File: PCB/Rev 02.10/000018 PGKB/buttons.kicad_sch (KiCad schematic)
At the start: 50 parts, among them U1 SN74HCS365PWR, U2 SN74HCS365PWR

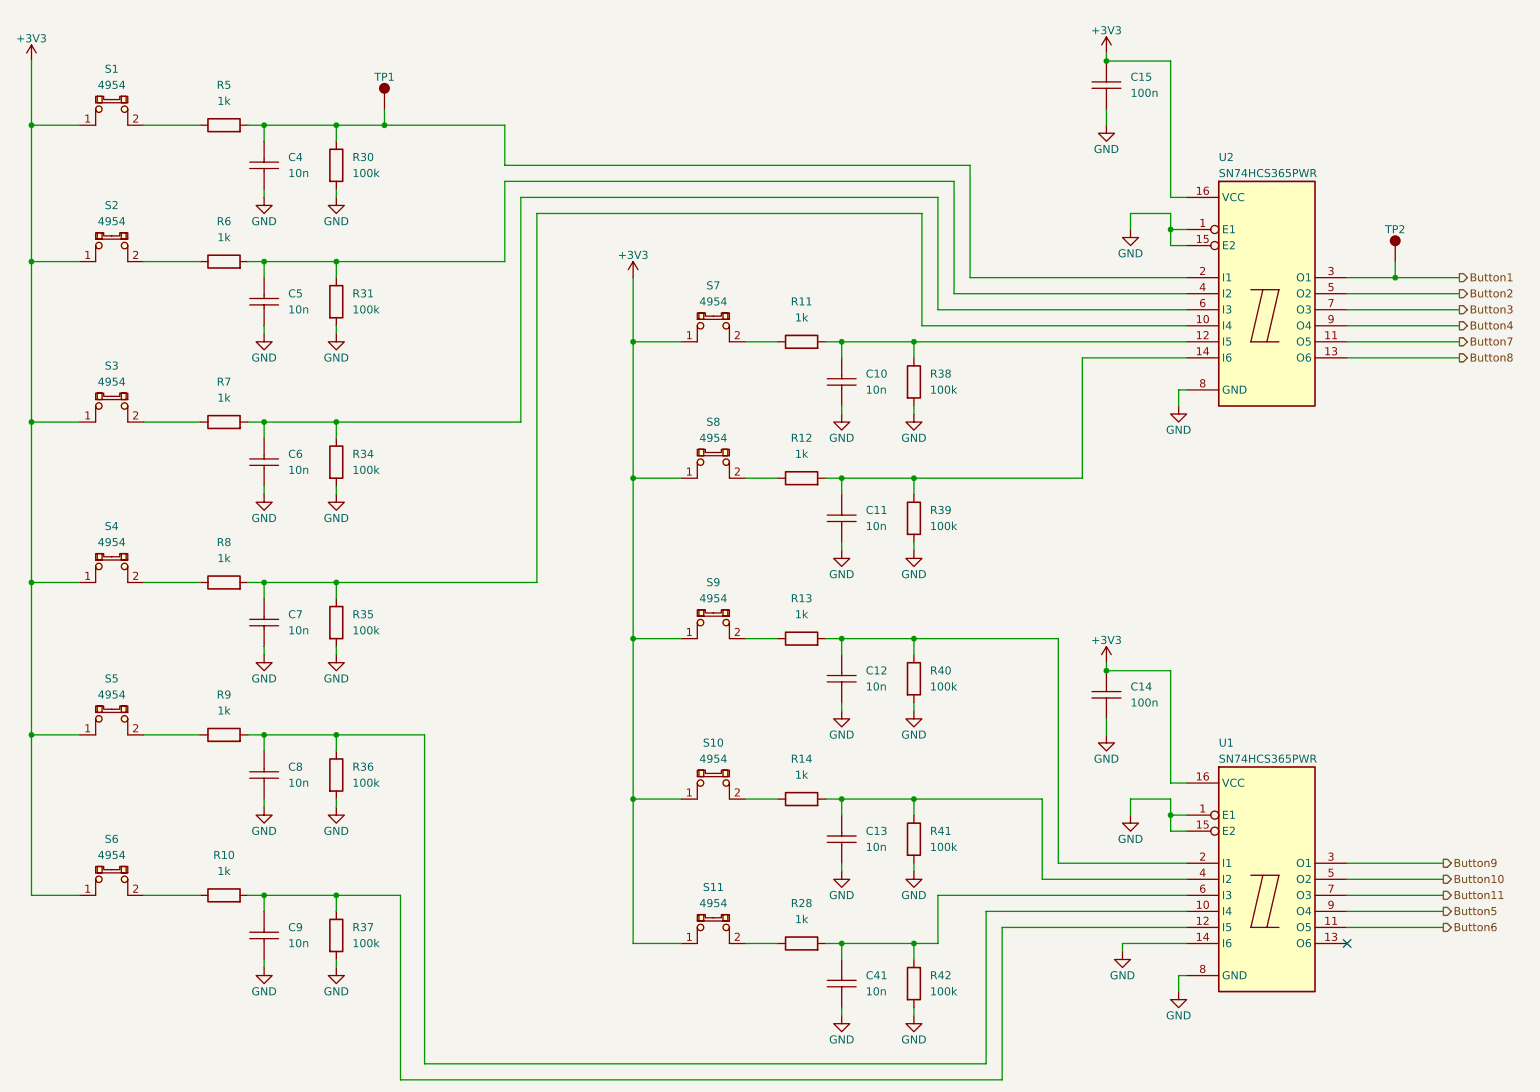
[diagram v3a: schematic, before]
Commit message: Resolved DRC problems
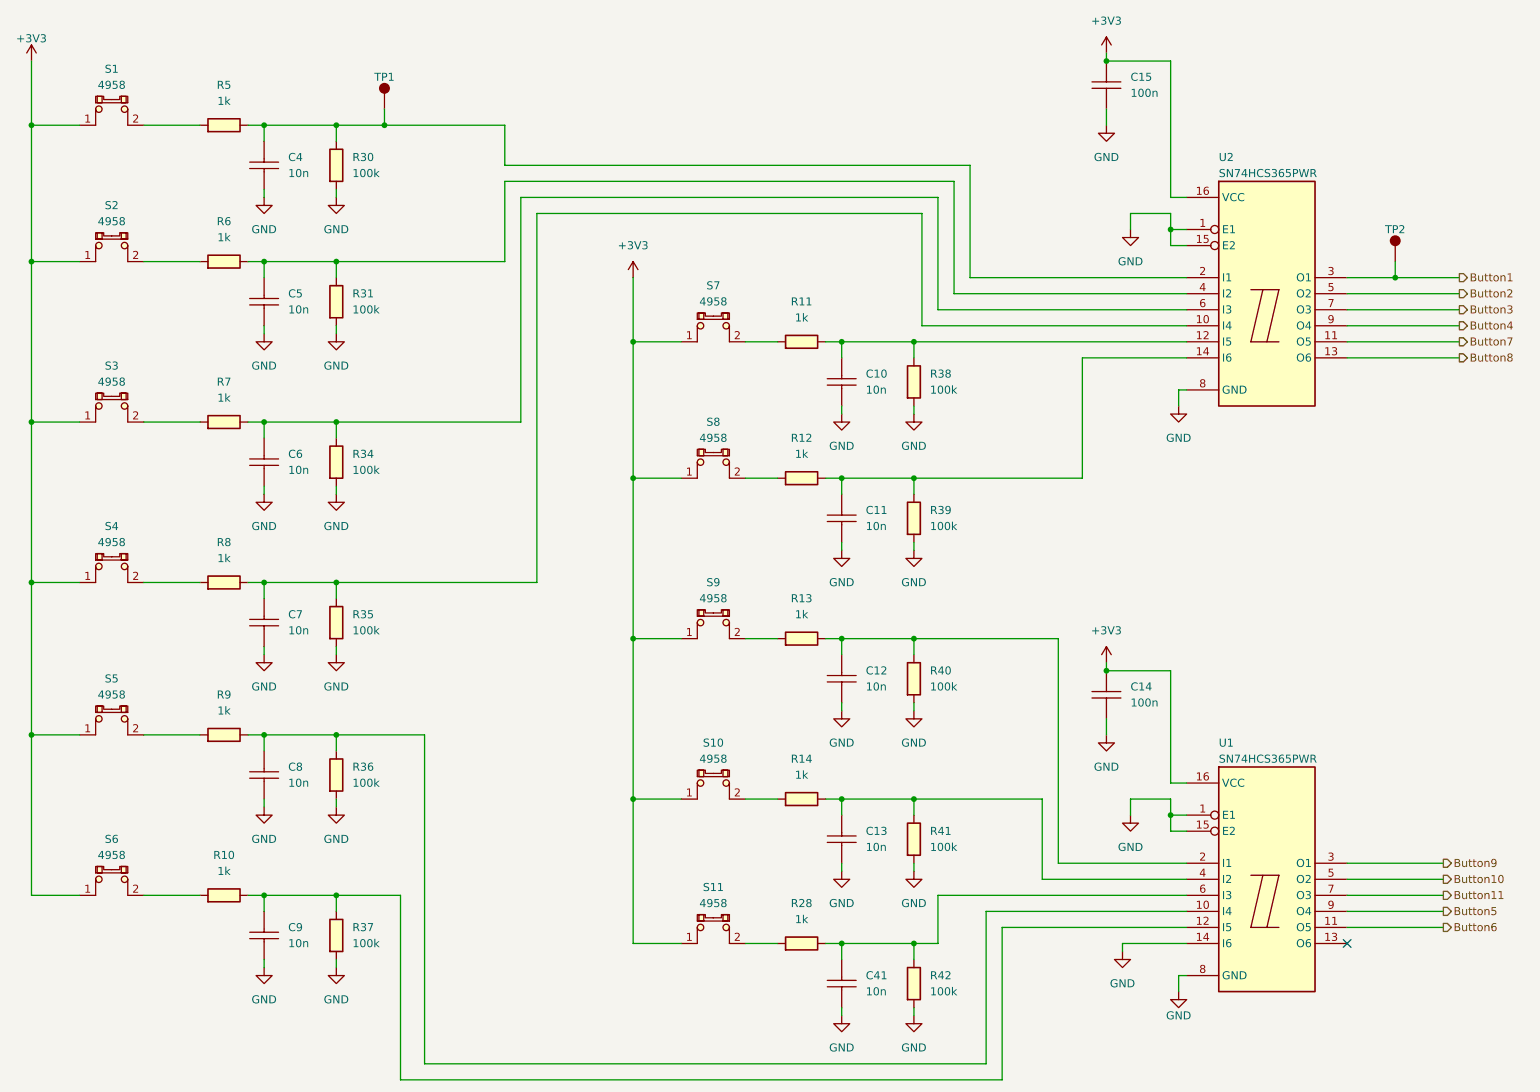
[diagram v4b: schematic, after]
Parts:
- C10, C11, C12, C13, C4, C41, C5, C6, C7, C8, C9: Code 10n -> (none)
- R10, R11, R12, R13, R14, R28, R5, R6, R7, R8, R9: Code 1k -> (none)
- S1, S10, S11, S2, S3, S4, S5, S6, S7, S8, S9: value 4954 -> 4958; symbol KD_Switch:Button_keyboard_socket_Adafruit_4958 -> KD_Switch:Button_keyboard_socket_MX_Adafruit_4958; MFG_PartNo 4954 -> 4958; Price 0.5 -> 0.45; Supplier_PartNo 1528-4954-ND -> 1528-4958-ND
- U1, U2: symbol KD_IC_Buffer_Driver_Interface:Schmitt_6CH_SN74HCS365PWR -> KD_IC_Buffer_Driver_Interface:Buffer_Schmitt_6CH_SN74HCS365PWR
